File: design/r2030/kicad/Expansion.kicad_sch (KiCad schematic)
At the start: 28 parts, among them IC7 74LS148, J3 Conn_02x32_Odd_Even, J3-X1 Conn_01x04_Male, J5 PWR, J6 Conn_01x04_Male

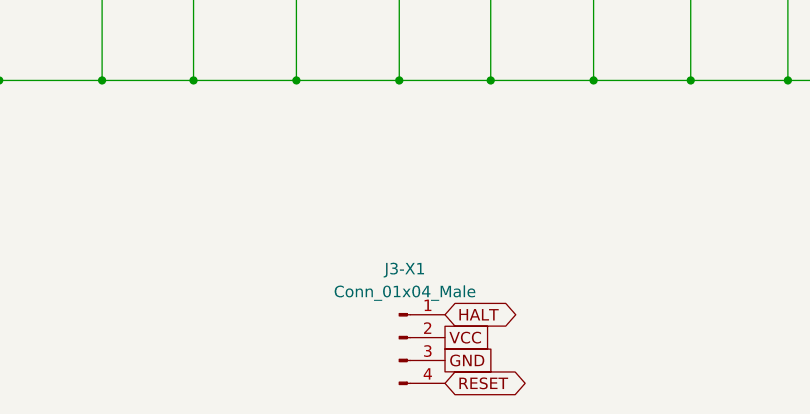
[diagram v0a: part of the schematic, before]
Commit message: Update to Kicad 7
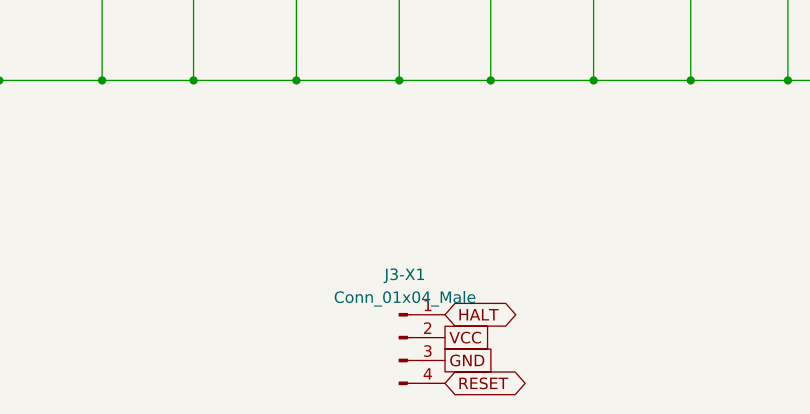
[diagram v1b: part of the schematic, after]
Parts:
- J3-X1, J6: symbol Connector:Conn_01x04_Male -> Connector:Conn_01x04_Pin

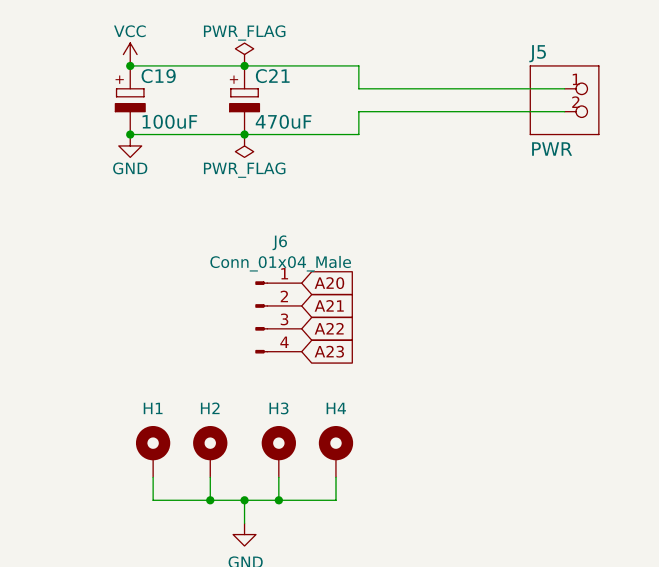
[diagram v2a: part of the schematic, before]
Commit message: EXPSEL on J6
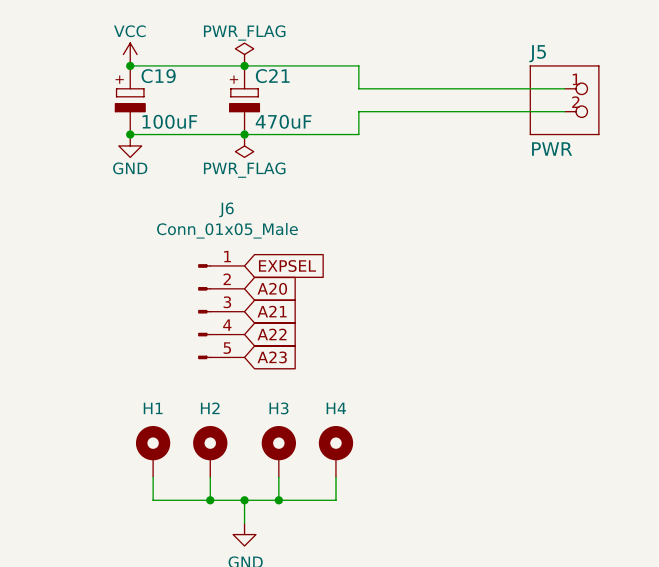
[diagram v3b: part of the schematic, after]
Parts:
- J6: value Conn_01x04_Male -> Conn_01x05_Male; footprint Connector_PinHeader_2.54mm:PinHeader_1x04_P2.54mm_Vertical -> Connector_PinHeader_2.54mm:PinHeader_1x05_P2.54mm_Vertical; symbol Connector:Conn_01x04_Pin -> Connector:Conn_01x05_Pin
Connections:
- net A20: now also J6.2 (Pin_2); no longer J6.1 (Pin_1)
- net A21: now also J6.3 (Pin_3); no longer J6.2 (Pin_2)
- net A22: now also J6.4 (Pin_4); no longer J6.3 (Pin_3)
- net A23: now also J6.5 (Pin_5); no longer J6.4 (Pin_4)
- net EXPSEL: now also J6.1 (Pin_1)
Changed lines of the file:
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@@
     )
   )
-  (global_label "A21" (shape input) (at 48.26 62.23 0) (fields_autoplaced)
-    (effects (font (size 1.27 1.27)) (justify left))
-    (property "Intersheetrefs" "${INTERSHEET_REFS}" (at 54.0986 62.23 0)
+  (global_label "A21" (shape input) (at 41.91 62.865 0) (fields_autoplaced)
+    (effects (font (size 1.27 1.27)) (justify left))
+    (property "Intersheetrefs" "${INTERSHEET_REFS}" (at 47.7486 62.865 0)
       (effects (font (size 1.27 1.27)) (justify left) hide)
     )
@@
     )
   )
+  (global_label "EXPSEL" (shape input) (at 41.91 57.785 0) (fields_autoplaced)
+    (effects (font (size 1.27 1.27)) (justify left))
+    (property "Intersheetrefs" "${INTERSHEET_REFS}" (at 51.2561 57.785 0)
+      (effects (font (size 1.27 1.27)) (justify left) hide)
+    )
+  )
   (global_label "E" (shape output) (at 227.33 53.34 0) (fields_autoplaced)
     (effects (font (size 1.27 1.27)) (justify left))
@@
     )
   )
-  (global_label "A20" (shape input) (at 48.26 59.69 0) (fields_autoplaced)
-    (effects (font (size 1.27 1.27)) (justify left))
-    (property "Intersheetrefs" "${INTERSHEET_REFS}" (at 54.0986 59.69 0)
+  (global_label "A20" (shape input) (at 41.91 60.325 0) (fields_autoplaced)
+    (effects (font (size 1.27 1.27)) (justify left))
+    (property "Intersheetrefs" "${INTERSHEET_REFS}" (at 47.7486 60.325 0)
       (effects (font (size 1.27 1.27)) (justify left) hide)
     )
@@
     )
   )
-  (global_label "A22" (shape input) (at 48.26 64.77 0) (fields_autoplaced)
-    (effects (font (size 1.27 1.27)) (justify left))
-    (property "Intersheetrefs" "${INTERSHEET_REFS}" (at 54.0986 64.77 0)
+  (global_label "A22" (shape input) (at 41.91 65.405 0) (fields_autoplaced)
+    (effects (font (size 1.27 1.27)) (justify left))
+    (property "Intersheetrefs" "${INTERSHEET_REFS}" (at 47.7486 65.405 0)
       (effects (font (size 1.27 1.27)) (justify left) hide)
     )
@@
     )
   )
-  (global_label "A23" (shape input) (at 48.26 67.31 0) (fields_autoplaced)
-    (effects (font (size 1.27 1.27)) (justify left))
-    (property "Intersheetrefs" "${INTERSHEET_REFS}" (at 54.0986 67.31 0)
+  (global_label "A23" (shape input) (at 41.91 67.945 0) (fields_autoplaced)
+    (effects (font (size 1.27 1.27)) (justify left))
+    (property "Intersheetrefs" "${INTERSHEET_REFS}" (at 47.7486 67.945 0)
       (effects (font (size 1.27 1.27)) (justify left) hide)
     )
@@
     )
   )
-  (symbol (lib_id "Connector:Conn_01x04_Pin") (at 43.18 62.23 0) (unit 1)
-    (in_bom yes) (on_board yes) (dnp no)
-    (property "Reference" "J6" (at 45.9232 55.0926 0)
-      (effects (font (size 1.27 1.27)))
-    )
-    (property "Value" "Conn_01x04_Male" (at 45.9232 57.404 0)
-      (effects (font (size 1.27 1.27)))
-    )
-    (property "Footprint" "Connector_PinHeader_2.54mm:PinHeader_1x04_P2.54mm_Vertical" (at 43.18 62.23 0)
-      (effects (font (size 1.27 1.27)) hide)
-    )
-    (property "Datasheet" "~" (at 43.18 62.23 0)
+  (symbol (lib_id "Connector:Conn_01x05_Pin") (at 36.83 62.865 0) (unit 1)
+    (in_bom yes) (on_board yes) (dnp no)
+    (property "Reference" "J6" (at 40.005 51.435 0)
+      (effects (font (size 1.27 1.27)))
+    )
+    (property "Value" "Conn_01x05_Male" (at 40.005 53.7464 0)
+      (effects (font (size 1.27 1.27)))
+    )
+    (property "Footprint" "Connector_PinHeader_2.54mm:PinHeader_1x05_P2.54mm_Vertical" (at 36.83 62.865 0)
+      (effects (font (size 1.27 1.27)) hide)
+    )
+    (property "Datasheet" "~" (at 36.83 62.865 0)
       (effects (font (size 1.27 1.27)) hide)
     )
@@
     (pin "3")
     (pin "4")
-    (instances
-      (project "rosco_m68k"
+    (pin "5")
+    (instances
+      (project "rosco_m68k"

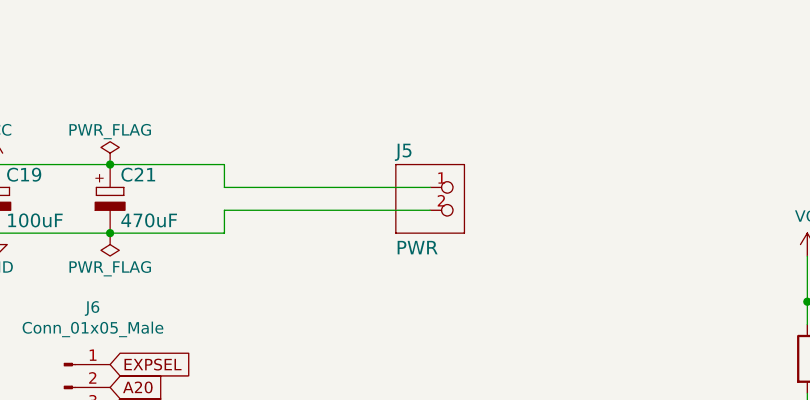
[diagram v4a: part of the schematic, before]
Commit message: Minor classic refresh for 2024 (#416)
* Minor classic refresh for 2024

* Add DC jack
* Silk cleanup
* Unify added memory expansion headers
* Minor routing cleanup
* QR code on silk

* Fix 2020 missing polarity symbol
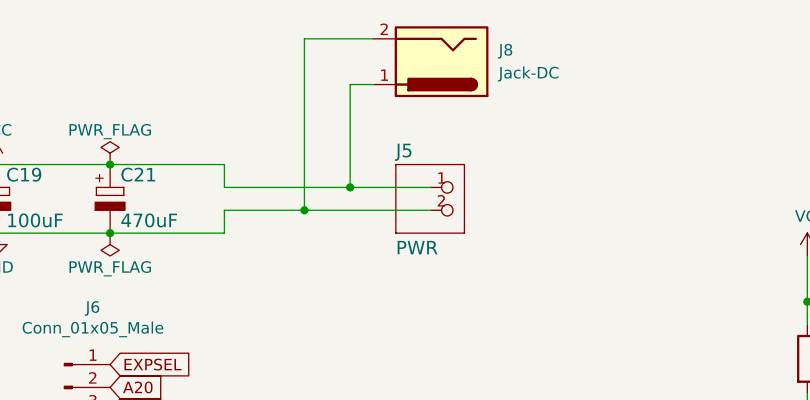
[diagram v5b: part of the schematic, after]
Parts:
- added J8: Jack-DC, Connector_BarrelJack:BarrelJack_Horizontal, symbol Connector:Jack-DC
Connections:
- net GND: now also J8.2
- net VCC: now also J8.1
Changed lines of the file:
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@@
   (title_block
     (title "ROSCO_M68K CLASSIC MC68030 EDITION")
-    (date "2023-12-10")
-    (rev "2.0")
+    (date "2024-03-09")
+    (rev "2.10")
     (company "The Really Old-School Company Limited")
     (comment 1 "OSHWA UK000006 (https://certification.oshwa.org/uk000006.html)")
     (comment 2 "See https://github.com/roscopeco/rosco_m68k/blob/master/LICENCE.hardware.txt")
     (comment 3 "Open Source Hardware licenced under CERN Open Hardware Licence")
-    (comment 4 "Copyright 2019-2023 Ross Bamford and Contributors")
+    (comment 4 "Copyright 2019-2024 Ross Bamford and Contributors")
   )
   (junction (at 38.1 83.82) (diameter 0) (color 0 0 0 0)
@@
   (junction (at 52.07 146.05) (diameter 0) (color 0 0 0 0)
   )
+  (junction (at 68.58 38.1) (diameter 0) (color 0 0 0 0)
+  )
   (junction (at 151.765 118.11) (diameter 0) (color 0 0 0 0)
   )
@@
   )
   (junction (at 139.7 118.11) (diameter 0) (color 0 0 0 0)
+  )
+  (junction (at 63.5 40.64) (diameter 0) (color 0 0 0 0)
   )
   (junction (at 241.3 27.94) (diameter 0) (color 0 0 0 0)
@@
     (stroke (width 0) (type default))
   )
+  (wire (pts (xy 68.58 38.1) (xy 54.61 38.1))
+    (stroke (width 0) (type default))
+  )
+  (wire (pts (xy 68.58 26.67) (xy 68.58 38.1))
+    (stroke (width 0) (type default))
+  )
   (wire (pts (xy 119.38 45.72) (xy 119.38 50.8))
     (stroke (width 0) (type default))
@@
     (stroke (width 0) (type default))
   )
+  (wire (pts (xy 71.12 21.59) (xy 63.5 21.59))
+    (stroke (width 0) (type default))
+  )
   (wire (pts (xy 41.91 83.82) (xy 41.91 86.36))
     (stroke (width 0) (type default))
@@
     (stroke (width 0) (type default))
   )
-  (wire (pts (xy 77.47 38.1) (xy 54.61 38.1))
+  (wire (pts (xy 77.47 38.1) (xy 68.58 38.1))
     (stroke (width 0) (type default))
   )
@@
     (stroke (width 0) (type default))
   )
+  (wire (pts (xy 71.12 26.67) (xy 68.58 26.67))
+    (stroke (width 0) (type default))
+  )
   (wire (pts (xy 257.81 48.26) (xy 257.81 120.65))
     (stroke (width 0) (type default))
@@
     (stroke (width 0) (type default))
   )
-  (wire (pts (xy 77.47 40.64) (xy 54.61 40.64))
+  (wire (pts (xy 77.47 40.64) (xy 63.5 40.64))
     (stroke (width 0) (type default))
   )
@@
     (stroke (width 0) (type default))
   )
+  (wire (pts (xy 63.5 40.64) (xy 54.61 40.64))
+    (stroke (width 0) (type default))
+  )
   (wire (pts (xy 106.68 118.11) (xy 95.25 118.11))
     (stroke (width 0) (type default))
@@
   )
   (wire (pts (xy 139.7 146.05) (xy 151.765 146.05))
+    (stroke (width 0) (type default))
+  )
+  (wire (pts (xy 63.5 21.59) (xy 63.5 40.64))
     (stroke (width 0) (type default))
   )
@@
         )
       )
+    )
+  )
+  (symbol (lib_id "Connector:Jack-DC") (at 78.74 24.13 180) (unit 1)
+    (in_bom yes) (on_board yes) (dnp no) (fields_autoplaced)
+    (property "Reference" "J8" (at 85.09 22.86 0)
+      (effects (font (size 1.27 1.27)) (justify right))
+    )
+    (property "Value" "Jack-DC" (at 85.09 25.4 0)
+      (effects (font (size 1.27 1.27)) (justify right))
+    )
+    (property "Footprint" "Connector_BarrelJack:BarrelJack_Horizontal" (at 77.47 23.114 0)
+      (effects (font (size 1.27 1.27)) hide)
+    )
+    (property "Datasheet" "~" (at 77.47 23.114 0)
+      (effects (font (size 1.27 1.27)) hide)
+    )
+    (pin "1")
+    (pin "2")
+    (instances
+      (project "rosco_m68k"
+        (path "/9031bb33-c6aa-4758-bf5c-3274ed3ebab7/00000000-0000-0000-0000-00005e53bc83"
+          (reference "J8") (unit 1)
+        )
+      )
+      (project "rosco_6502"
+        (path "/e63e39d7-6ac0-4ffd-8aa3-1841a4541b55"
+          (reference "J7") (unit 1)
+        )
+      )
